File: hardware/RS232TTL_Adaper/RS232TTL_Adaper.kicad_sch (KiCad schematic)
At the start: 8 parts, among them J1 DB25_Male, J2 Conn_01x05, U1 MAX232N

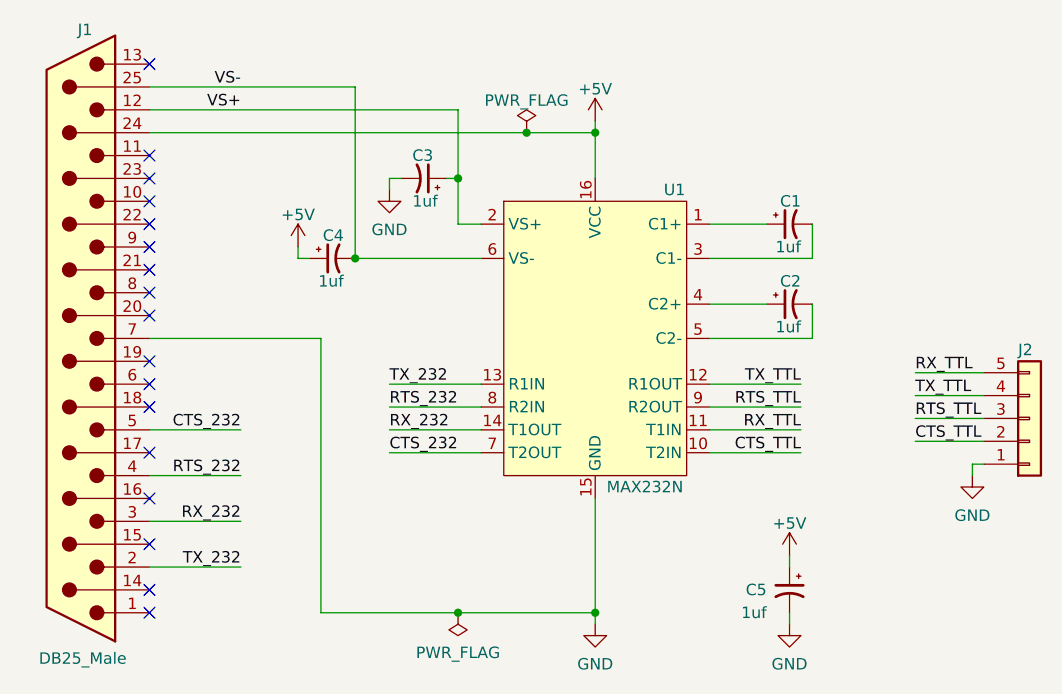
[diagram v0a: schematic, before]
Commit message: remove connection to +/- 12v
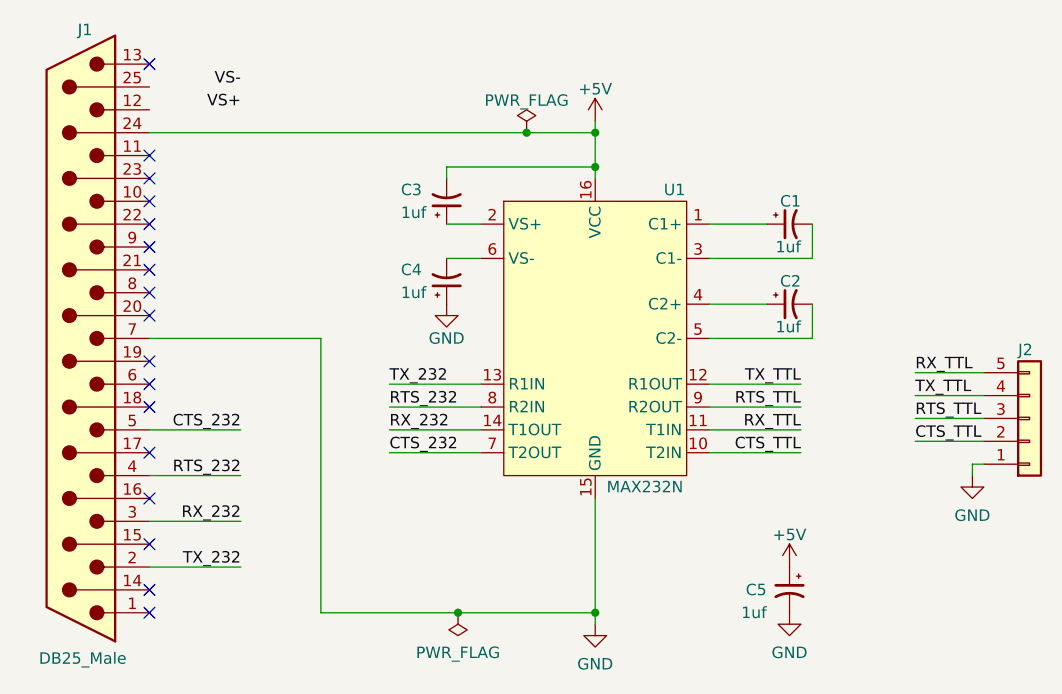
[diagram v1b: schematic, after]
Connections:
- net +5V: now also C3.2; no longer C4.1
- net GND: now also C4.1; no longer C3.2
- net VS+: no longer C3.1, J1.12, U1.2 (VS+)
- net VS-: no longer C4.2, J1.25 (P25), U1.6 (VS-)
- new net: C3.1, U1.2 (VS+)
- new net: C4.2, U1.6 (VS-)
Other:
- moved on the sheet: C3, C4
